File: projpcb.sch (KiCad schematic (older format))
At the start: 1 part

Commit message: schematic so far
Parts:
- added U?: CD74HC4067, symbol CD74HC4067
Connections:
- new net +3V3: U?.24 (VCC)
- new net GND: U?.12 (GND)
- new net Phototransistors/S1: U?.9 (I0)
- new net Phototransistors/S10: U?.22 (I9)
- new net Phototransistors/S11: U?.21 (I10)
- new net Phototransistors/S12: U?.20 (I11)
- new net Phototransistors/S13: U?.19 (I12)
- new net Phototransistors/S14: U?.18 (I13)
- new net Phototransistors/S15: U?.17 (I14)
- new net Phototransistors/S2: U?.8 (I1)
- new net Phototransistors/S3: U?.7 (I2)
- new net Phototransistors/S4: U?.6 (I3)
- new net Phototransistors/S5: U?.5 (I4)
- new net Phototransistors/S6: U?.4 (I5)
- new net Phototransistors/S7: U?.3 (I6)
- new net Phototransistors/S8: U?.2 (I7)
- new net Phototransistors/S9: U?.23 (I8)
- no-connect marks 0 -> 1
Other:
- moved on the sheet: U?
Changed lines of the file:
@@
 LIBS:valves
 LIBS:teensy_3.1
+LIBS:sfh3711
+LIBS:cd74hc4067
+LIBS:projpcb-cache
 EELAYER 25 0
 EELAYER END
 $Descr A4 11693 8268
 encoding utf-8
-Sheet 1 1
+Sheet 1 2
 Title ""
 Date ""
@@
 L Teensy_3.1 U?
 U 1 1 56B935F7
-P 3175 3500
-F 0 "U?" H 3225 4550 60  0000 C CNN
-F 1 "Teensy_3.1" H 3275 5000 60  0000 C CNN
-F 2 "" H 3275 3500 60  0000 C CNN
-F 3 "" H 3275 3500 60  0000 C CNN
-	1    3175 3500
+P 2025 2450
+F 0 "U?" H 2075 3500 60  0000 C CNN
+F 1 "Teensy_3.1" H 2125 3950 60  0000 C CNN
+F 2 "" H 2125 2450 60  0000 C CNN
+F 3 "" H 2125 2450 60  0000 C CNN
+	1    2025 2450
 	1    0    0    -1
 $EndComp
+$Sheet
+S 7150 1275 2700 2000
+U 56B9494D
+F0 "Phototransistors" 60
+F1 "phototransistors.sch" 60
+F2 "S1" O L 7150 1375 60
+F3 "S2" O L 7150 1500 60
+F4 "S3" O L 7150 1625 60
+F5 "S4" O L 7150 1750 60
+F6 "S5" O L 7150 1875 60
+F7 "S6" O L 7150 2000 60
+F8 "S7" O L 7150 2125 60
+F9 "S8" O L 7150 2250 60
+F10 "S9" O L 7150 2375 60
+F11 "S10" O L 7150 2500 60
+F12 "S11" O L 7150 2625 60
+F13 "S12" O L 7150 2750 60
+F14 "S13" O L 7150 2875 60
+F15 "S14" O L 7150 3000 60
+F16 "S15" O L 7150 3125 60
+$EndSheet
+$Comp
+L CD74HC4067 U?
+U 1 1 56B96E51
+P 5975 1450
+F 0 "U?" H 5975 1350 60  0000 C CNN
+F 1 "CD74HC4067" H 5975 1450 60  0000 C CNN
+F 2 "" H 5975 1450 60  0000 C CNN
+F 3 "" H 5975 1450 60  0000 C CNN
+	1    5975 1450
+	1    0    0    -1
+$EndComp
+Wire Wire Line
+	7150 1375 6600 1375
+Wire Wire Line
+	6600 1375 6600 1600
+Wire Wire Line
+	6600 1600 6525 1600
+Wire Wire Line
+	7150 1500 6625 1500
+Wire Wire Line
+	6625 1500 6625 1700
+Wire Wire Line
+	6625 1700 6525 1700
+Wire Wire Line
+	7150 1625 6650 1625
+Wire Wire Line
+	6650 1625 6650 1800
+Wire Wire Line
+	6650 1800 6525 1800
+Wire Wire Line
+	7150 1750 6675 1750
+Wire Wire Line
+	6675 1750 6675 1900
+Wire Wire Line
+	6675 1900 6525 1900
+Wire Wire Line
+	7150 1875 6700 1875
+Wire Wire Line
+	6700 1875 6700 2000
+Wire Wire Line
+	6700 2000 6525 2000
+Wire Wire Line
+	7150 2000 6725 2000
+Wire Wire Line
+	6725 2000 6725 2100
+Wire Wire Line
+	6725 2100 6525 2100
+Wire Wire Line
+	7150 2125 6750 2125
+Wire Wire Line
+	6750 2125 6750 2200
+Wire Wire Line
+	6750 2200 6525 2200
+Wire Wire Line
+	7150 2250 6775 2250
+Wire Wire Line
+	6775 2250 6775 2300
+Wire Wire Line
+	6775 2300 6525 2300
+Wire Wire Line
+	7150 2375 6800 2375
+Wire Wire Line
+	6800 2375 6800 2400
+Wire Wire Line
+	6800 2400 6525 2400
+Wire Wire Line
+	7150 2500 6525 2500
+Wire Wire Line
+	7150 2625 6775 2625
+Wire Wire Line
+	6775 2625 6775 2600
+Wire Wire Line
+	6775 2600 6525 2600
+Wire Wire Line
+	7150 2750 6750 2750
+Wire Wire Line
+	6750 2750 6750 2700
+Wire Wire Line
+	6750 2700 6525 2700
+Wire Wire Line
+	7150 2875 6725 2875
+Wire Wire Line
+	6725 2875 6725 2800
+Wire Wire Line
+	6725 2800 6525 2800
+Wire Wire Line
+	7150 3000 6700 3000
+Wire Wire Line
+	6700 3000 6700 2900
+Wire Wire Line
+	6700 2900 6525 2900
+Wire Wire Line
+	7150 3125 6675 3125
+Wire Wire Line
+	6675 3125 6675 3000
+Wire Wire Line
+	6675 3000 6525 3000
+NoConn ~ 5425 1650
+$Comp
+L GND #PWR?
+U 1 1 56B97CB9
+P 5425 1850
+F 0 "#PWR?" H 5425 1600 50  0001 C CNN
+F 1 "GND" H 5425 1700 50  0000 C CNN
+F 2 "" H 5425 1850 50  0000 C CNN
+F 3 "" H 5425 1850 50  0000 C CNN
+	1    5425 1850
+	1    0    0    -1
+$EndComp
+$Comp
+L +3.3V #PWR?
+U 1 1 56B97DF5
+P 5425 1550
+F 0 "#PWR?" H 5425 1400 50  0001 C CNN
+F 1 "+3.3V" H 5425 1690 50  0000 C CNN
+F 2 "" H 5425 1550 50  0000 C CNN
+F 3 "" H 5425 1550 50  0000 C CNN
+	1    5425 1550
+	1    0    0    -1
+$EndComp

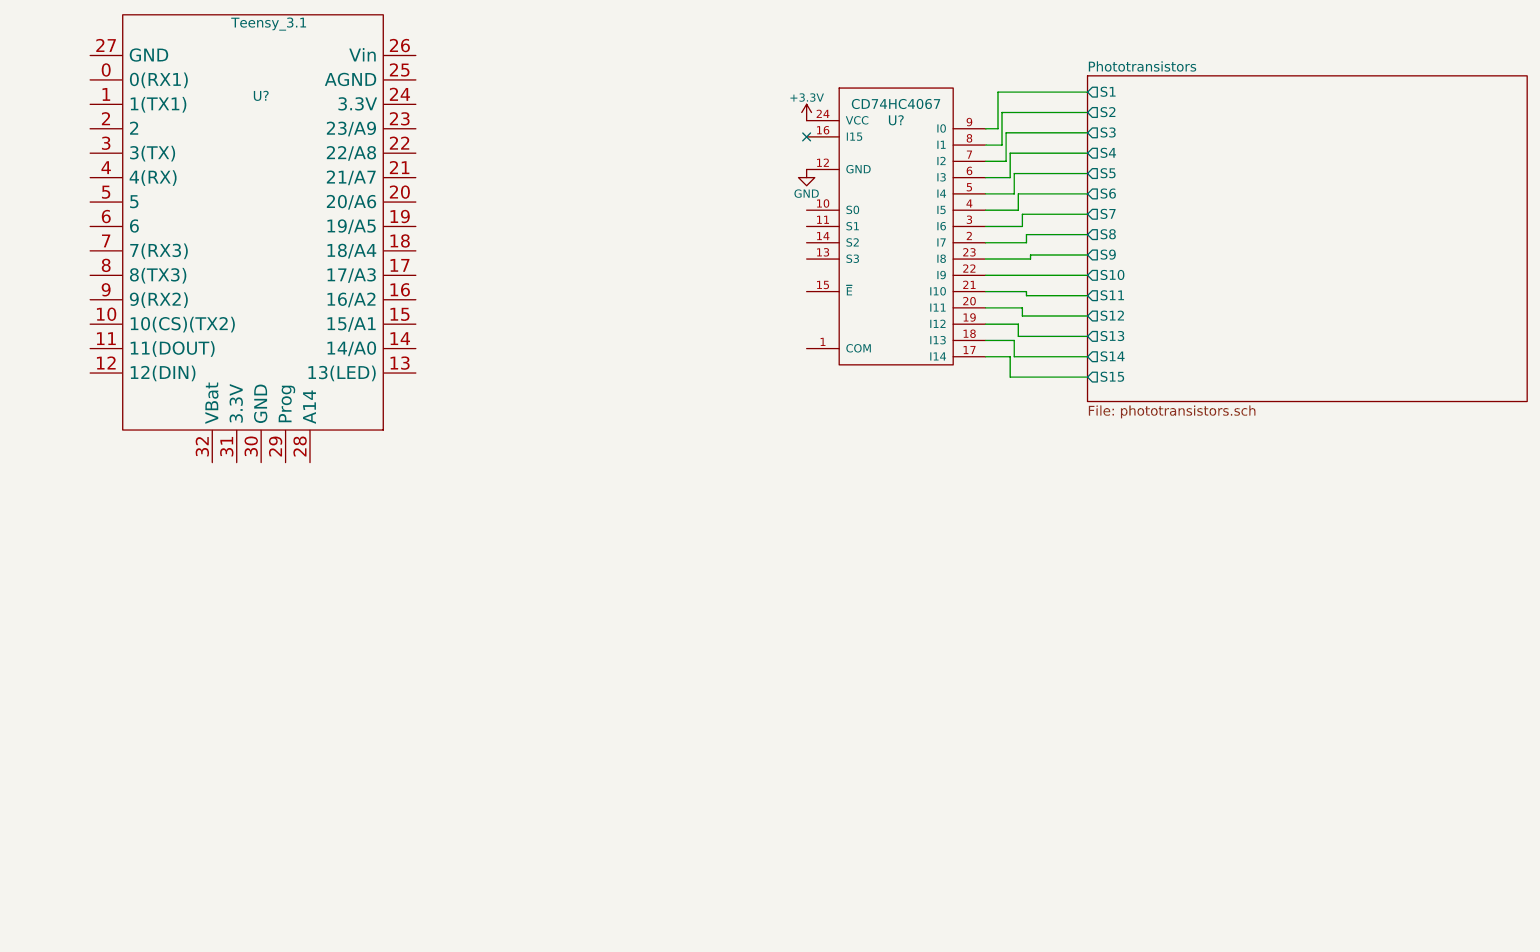
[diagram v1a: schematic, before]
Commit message: Progress on schematic, phototransistor array + analog frontend complete
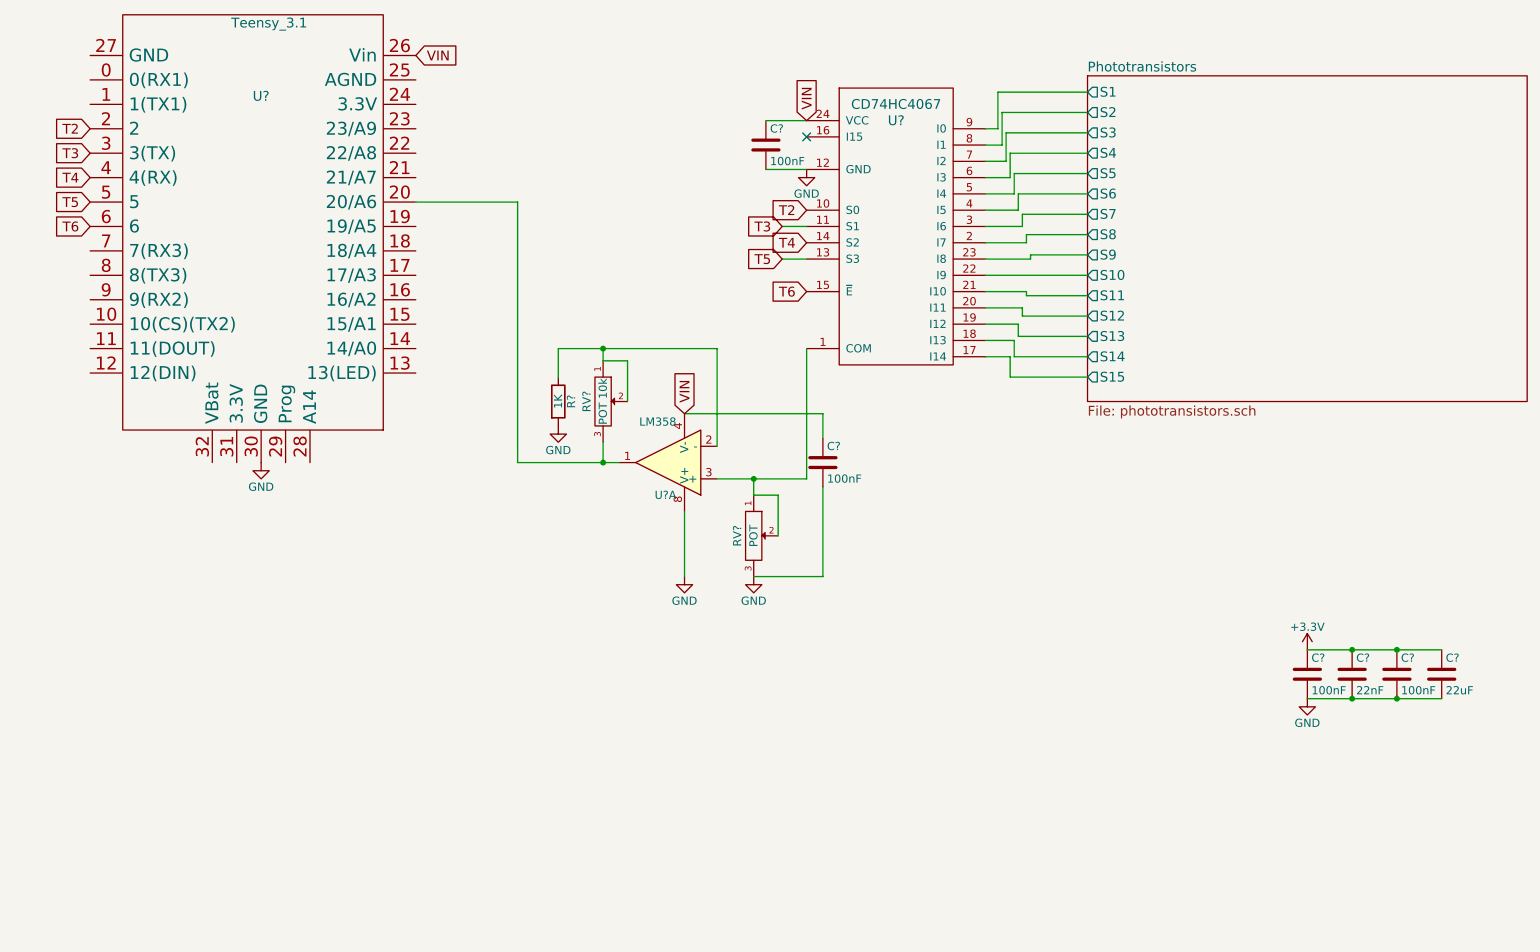
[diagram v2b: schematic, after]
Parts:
- added C? (x3): 100nF, Capacitors_SMD:C_0805_HandSoldering, symbol C
- added C?: 100nF, symbol C
- added C?: 22nF, Capacitors_SMD:C_0805_HandSoldering, symbol C
- added C?: 22uF, Capacitors_SMD:C_0805_HandSoldering, symbol C
- added R?: 1K, Resistors_SMD:R_0805_HandSoldering, symbol R
- added RV?: POT, symbol POT
- added RV?: POT 10k, symbol POT
- added U?: LM358, Housings_DIP:DIP-8_W7.62mm, symbol LM358
- U?: footprint (none) -> Teensy-3:Teensy-3.1
- U?: footprint (none) -> Housings_DIP:DIP-24_W10.16mm
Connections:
- net +3V3: now also C?.1, C?.1, C?.1, C?.1; no longer U?.24 (VCC)
- net GND: now also U?.30 (GND), C?.2, C?.2, C?.2, C?.2, C?.2, C?.2, R?.2, RV?.3, U?.8 (V+)
- net T2: now reaches U?.2
- net T2: now also U?.10 (S0)
- net at U?.20 (20/A6): now also RV?.3, U?.1
- net VIN: now reaches U?.26 (Vin)
- net VIN: now also U?.24 (VCC), C?.1, C?.1, U?.4 (V-)
- net T3: now reaches U?.3 (3(TX))
- net T3: now also U?.11 (S1)
- net T4: now reaches U?.4 (4(RX))
- net T4: now also U?.14 (S2)
- net T5: now reaches U?.5
- net T5: now also U?.13 (S3)
- net T6: now reaches U?.6
- net T6: now also U?.15 (~E)
- net at U?.1 (COM): now also RV?.1, RV?.2, U?.3 (+)
- new net: R?.1, RV?.1, RV?.2, U?.2 (-)

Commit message: Draft version v1 of Schematic
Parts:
- added CON1, CON2: BARREL_JACK, Connect:BARREL_JACK, symbol BARREL_JACK
- added P1: CONN_01X02, Pin_Headers:Pin_Header_Straight_1x02, symbol CONN_01X02
- added P2: CONN_01X02, Pin_Headers:Pin_Header_Angled_1x02, symbol CONN_01X02
- added Q16: Q_NMOS_GSD, TO_SOT_Packages_SMD:SOT-23_Handsoldering, symbol Q_NMOS_GSD
- added R2: 6.8K, Resistors_SMD:R_0805_HandSoldering, symbol R
- added U4: CL520, TO_SOT_Packages_THT:TO-92_Inline_Narrow_Oval, symbol CL520
- C2: renamed from C?; footprint (none) -> Capacitors_SMD:C_0805_HandSoldering
- RV1, RV2: renamed from RV?; footprint (none) -> Potentiometers:Potentiometer_Trimmer-Suntan-TSR-3386P
- gave numbers to parts that had none: 9
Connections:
- net +3V3: now also U1.31 (3.3V)
- net GND: now also CON1.2, P2.1 (P1), Q16.2 (S), R2.2, U4.1 (GND)
- net VIN: now also P1.1 (P1), U4.3 (VDD)
- net HEAT: now reaches U1.7 (7(RX3))
- net HEAT: now also Q16.1 (G)
- new net: CON2.2, Q16.3 (D)
- new net: P2.2 (P2), U4.2 (OUT)
- new net HEATER_PWR: CON1.1, CON2.1
- new net TEMP_S: P1.2 (P2), R2.1
- no-connect marks 1 -> 2

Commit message: Board design V1
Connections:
- net TEMP_S: now also U1.21 (21/A7)
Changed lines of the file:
@@
 	0    1    1    0
 $EndComp
-Wire Wire Line
-	7150 1375 6600 1375
-Wire Wire Line
-	6600 1375 6600 1600
-Wire Wire Line
-	6600 1600 6525 1600
-Wire Wire Line
-	7150 1500 6625 1500
-Wire Wire Line
-	6625 1500 6625 1700
-Wire Wire Line
-	6625 1700 6525 1700
-Wire Wire Line
-	7150 1625 6650 1625
-Wire Wire Line
-	6650 1625 6650 1800
-Wire Wire Line
-	6650 1800 6525 1800
-Wire Wire Line
-	7150 1750 6675 1750
-Wire Wire Line
-	6675 1750 6675 1900
-Wire Wire Line
-	6675 1900 6525 1900
-Wire Wire Line
-	7150 1875 6700 1875
-Wire Wire Line
-	6700 1875 6700 2000
-Wire Wire Line
-	6700 2000 6525 2000
-Wire Wire Line
-	7150 2000 6725 2000
-Wire Wire Line
-	6725 2000 6725 2100
-Wire Wire Line
-	6725 2100 6525 2100
-Wire Wire Line
-	7150 2125 6750 2125
-Wire Wire Line
-	6750 2125 6750 2200
-Wire Wire Line
-	6750 2200 6525 2200
-Wire Wire Line
-	7150 2250 6775 2250
-Wire Wire Line
-	6775 2250 6775 2300
-Wire Wire Line
-	6775 2300 6525 2300
-Wire Wire Line
-	7150 2375 6800 2375
-Wire Wire Line
-	6800 2375 6800 2400
-Wire Wire Line
-	6800 2400 6525 2400
-Wire Wire Line
-	7150 2500 6525 2500
-Wire Wire Line
-	7150 2625 6775 2625
-Wire Wire Line
-	6775 2625 6775 2600
-Wire Wire Line
-	6775 2600 6525 2600
-Wire Wire Line
-	7150 2750 6750 2750
-Wire Wire Line
-	6750 2750 6750 2700
-Wire Wire Line
-	6750 2700 6525 2700
-Wire Wire Line
-	7150 2875 6725 2875
-Wire Wire Line
-	6725 2875 6725 2800
-Wire Wire Line
-	6725 2800 6525 2800
-Wire Wire Line
-	7150 3000 6700 3000
-Wire Wire Line
-	6700 3000 6700 2900
-Wire Wire Line
-	6700 2900 6525 2900
-Wire Wire Line
-	7150 3125 6675 3125
-Wire Wire Line
-	6675 3125 6675 3000
-Wire Wire Line
-	6675 3000 6525 3000
-Wire Wire Line
-	4875 3750 5100 3750
-Wire Wire Line
-	5100 3750 5425 3750
-Wire Wire Line
-	5100 3850 5100 3750
-Connection ~ 5100 3750
-Wire Wire Line
-	5100 3850 5250 3850
-Wire Wire Line
-	4675 4350 4675 3950
 $Comp
 L GND #PWR7
@@
 	0    1    1    0
 $EndComp
-Wire Wire Line
-	4175 3025 4325 3025
-Wire Wire Line
-	4325 3025 4325 3275
-Wire Wire Line
-	4175 3025 4175 2950
-Wire Wire Line
-	3900 2950 4175 2950
-Wire Wire Line
-	4175 2950 4875 2950
-Wire Wire Line
-	4875 2950 4875 3550
-Wire Wire Line
-	4175 3525 4175 3650
-Wire Wire Line
-	3650 3650 4175 3650
-Wire Wire Line
-	4175 3650 4275 3650
-Wire Wire Line
-	5425 3750 5425 2950
-Wire Wire Line
-	5250 3850 5250 4100
 $Comp
 L R R1
@@
 	1    0    0    -1
 $EndComp
-Wire Wire Line
-	3900 2950 3900 3125
-Connection ~ 4175 2950
 $Comp
 L GND #PWR5
@@
 	1    0    0    -1
 $EndComp
-Wire Wire Line
-	3650 3650 3650 2050
-Wire Wire Line
-	3650 2050 3025 2050
-Connection ~ 4175 3650
 Text GLabel 5425 1550 1    60   Input ~ 0
 VIN
@@
 Text GLabel 5425 2600 0    60   Input ~ 0
 T6
-Wire Wire Line
-	5425 2400 5275 2400
-Wire Wire Line
-	5275 2200 5425 2200
 $Comp
 L GND #PWR4
@@
 	1    0    0    -1
 $EndComp
-Wire Wire Line
-	5175 1550 5425 1550
-Wire Wire Line
-	5425 1850 5175 1850
 $Comp
 L C C2
@@
 	1    0    0    -1
 $EndComp
-Wire Wire Line
-	5525 3500 5525 3350
-Wire Wire Line
-	5525 3350 4675 3350
-Wire Wire Line
-	5525 3800 5525 4350
-Wire Wire Line
-	5525 4350 5100 4350
 $Comp
 L C C3
@@
 	1    0    0    -1
 $EndComp
-Wire Wire Line
-	8500 4800 8775 4800
-Wire Wire Line
-	8775 4800 9050 4800
-Wire Wire Line
-	9050 4800 9325 4800
-Connection ~ 8775 4800
 $Comp
 L GND #PWR13
@@
 	1    0    0    -1
 $EndComp
-Wire Wire Line
-	8500 5100 8775 5100
-Wire Wire Line
-	8775 5100 9050 5100
-Wire Wire Line
-	9050 5100 9325 5100
-Connection ~ 8775 5100
 $Comp
 L C C6
@@
 	1    0    0    -1
 $EndComp
-Connection ~ 9050 4800
-Connection ~ 9050 5100
 $Comp
 L +3.3V #PWR3
@@
 	-1   0    0    1
 $EndComp
-Wire Wire Line
-	1925 3750 1925 3650
 NoConn ~ 3025 3100
 $Comp
@@
 Text GLabel 1200 4150 2    60   Input ~ 0
 HEATER_PWR
-Wire Wire Line
-	1275 4425 1275 4350
-Wire Wire Line
-	1275 4350 1200 4350
 $Comp
 L R R2
@@
 Text GLabel 5125 5925 0    60   Input ~ 0
 VIN
-Wire Wire Line
-	5125 5925 5150 5925
-Wire Wire Line
-	5150 5925 5150 5975
 $Comp
 L CL520 U4
@@
 	1    0    0    -1
 $EndComp
+Text GLabel 3025 1900 2    60   Input ~ 0
+TEMP_S
+Wire Wire Line
+	7150 1375 6600 1375
+Wire Wire Line
+	6600 1375 6600 1600
+Wire Wire Line
+	6600 1600 6525 1600
+Wire Wire Line
+	7150 1500 6625 1500
+Wire Wire Line
+	6625 1500 6625 1700
+Wire Wire Line
+	6625 1700 6525 1700
+Wire Wire Line
+	7150 1625 6650 1625
+Wire Wire Line
+	6650 1625 6650 1800
+Wire Wire Line
+	6650 1800 6525 1800
+Wire Wire Line
+	7150 1750 6675 1750
+Wire Wire Line
+	6675 1750 6675 1900
+Wire Wire Line
+	6675 1900 6525 1900
+Wire Wire Line
+	7150 1875 6700 1875
+Wire Wire Line
+	6700 1875 6700 2000
+Wire Wire Line
+	6700 2000 6525 2000
+Wire Wire Line
+	7150 2000 6725 2000
+Wire Wire Line
+	6725 2000 6725 2100
+Wire Wire Line
+	6725 2100 6525 2100
+Wire Wire Line
+	7150 2125 6750 2125
+Wire Wire Line
+	6750 2125 6750 2200
+Wire Wire Line
+	6750 2200 6525 2200
+Wire Wire Line
+	7150 2250 6775 2250
+Wire Wire Line
+	6775 2250 6775 2300
+Wire Wire Line
+	6775 2300 6525 2300
+Wire Wire Line
+	7150 2375 6800 2375
+Wire Wire Line
+	6800 2375 6800 2400
+Wire Wire Line
+	6800 2400 6525 2400
+Wire Wire Line
+	7150 2500 6525 2500
+Wire Wire Line
+	7150 2625 6775 2625
+Wire Wire Line
+	6775 2625 6775 2600
+Wire Wire Line
+	6775 2600 6525 2600
+Wire Wire Line
+	7150 2750 6750 2750
+Wire Wire Line
+	6750 2750 6750 2700
+Wire Wire Line
+	6750 2700 6525 2700
+Wire Wire Line
+	7150 2875 6725 2875
+Wire Wire Line
+	6725 2875 6725 2800
+Wire Wire Line
+	6725 2800 6525 2800
+Wire Wire Line
+	7150 3000 6700 3000
+Wire Wire Line
+	6700 3000 6700 2900
+Wire Wire Line
+	6700 2900 6525 2900
+Wire Wire Line
+	7150 3125 6675 3125
+Wire Wire Line
+	6675 3125 6675 3000
+Wire Wire Line
+	6675 3000 6525 3000
+Wire Wire Line
+	4875 3750 5425 3750
+Wire Wire Line
+	5100 3850 5100 3750
+Connection ~ 5100 3750
+Wire Wire Line
+	5100 3850 5250 3850
+Wire Wire Line
+	4675 4350 4675 3950
+Wire Wire Line
+	4175 3025 4325 3025
+Wire Wire Line
+	4325 3025 4325 3275
+Wire Wire Line
+	4175 3025 4175 2950
+Wire Wire Line
+	3900 2950 4875 2950
+Wire Wire Line
+	4875 2950 4875 3550
+Wire Wire Line
+	4175 3525 4175 3650
+Wire Wire Line
+	3650 3650 4275 3650
+Wire Wire Line
+	5425 3750 5425 2950
+Wire Wire Line
+	5250 3850 5250 4100
+Wire Wire Line
+	3900 2950 3900 3125
+Connection ~ 4175 2950
+Wire Wire Line
+	3650 3650 3650 2050
+Wire Wire Line
+	3650 2050 3025 2050
+Connection ~ 4175 3650
+Wire Wire Line
+	5425 2400 5275 2400
+Wire Wire Line
+	5275 2200 5425 2200
+Wire Wire Line
+	5175 1550 5425 1550
+Wire Wire Line
+	5425 1850 5175 1850
+Wire Wire Line
+	5525 3500 5525 3350
+Wire Wire Line
+	5525 3350 4675 3350
+Wire Wire Line
+	5525 3800 5525 4350
+Wire Wire Line
+	5525 4350 5100 4350
+Wire Wire Line
+	8500 4800 9325 4800
+Connection ~ 8775 4800
+Wire Wire Line
+	8500 5100 9325 5100
+Connection ~ 8775 5100
+Connection ~ 9050 4800
+Connection ~ 9050 5100
+Wire Wire Line
+	1925 3750 1925 3650
+Wire Wire Line
+	1275 4425 1275 4350
+Wire Wire Line
+	1275 4350 1200 4350
+Wire Wire Line
+	5125 5925 5150 5925
+Wire Wire Line
+	5150 5925 5150 5975
 $EndSCHEMATC
